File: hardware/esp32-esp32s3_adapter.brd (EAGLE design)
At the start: 21.9 x 26.9 mm, 5 parts, among them U1 ESP32-S3-WROOM-1-N16R2, U2 ESP32-WROOM-32E_(16MB)

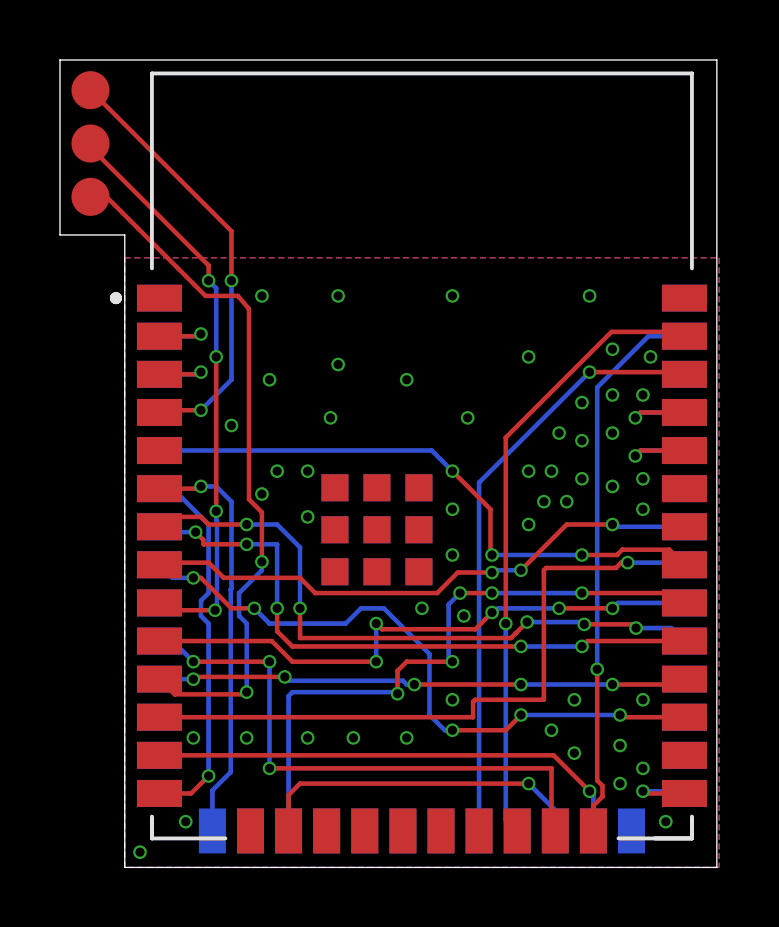
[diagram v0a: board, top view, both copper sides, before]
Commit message: Added RevB of ESP32toESP32S3 V1.4 and 2.0
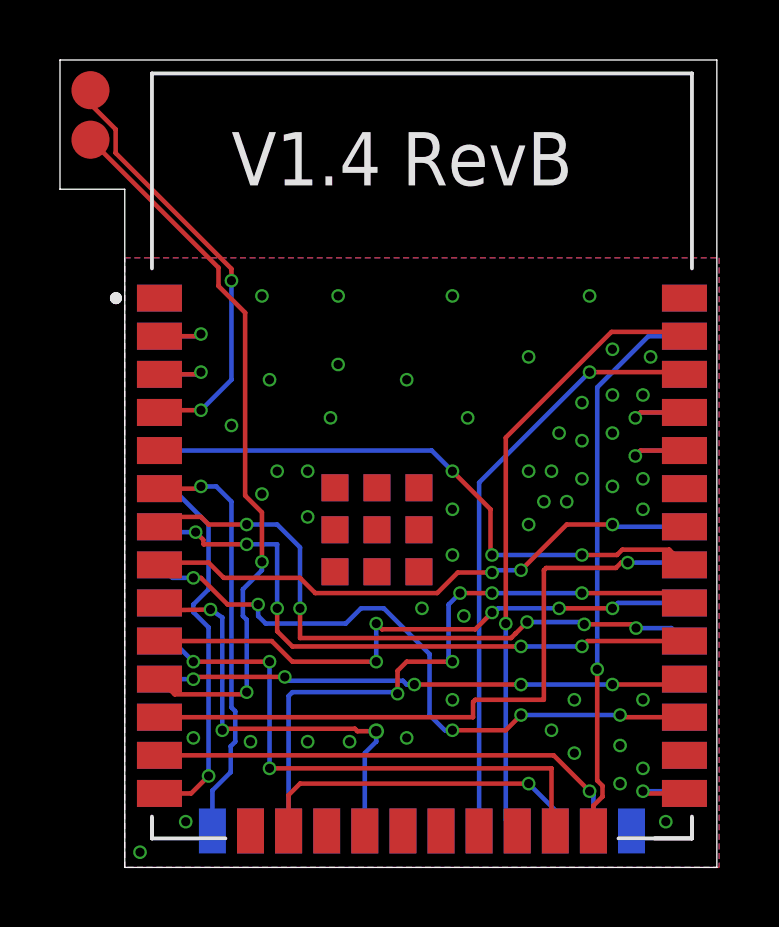
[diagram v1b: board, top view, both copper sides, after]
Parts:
- removed TP3: TPB1,27, testpad:B1,27
- moved TP1 1.91 mm to (2.41, 77.3)
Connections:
- net SQL: now also U1.19; no longer TP3.TP
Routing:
- net SQL: track 19.3 -> 14.7 mm, vias 4 -> 3
- net AF_OUT: track 23.4 -> 24.2 mm
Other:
- outline, holes or cut-outs redrawn
- board text added: "V1.4 RevB"

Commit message: RevC of ESP32-ESP32S3 Adapter SCH/PCB
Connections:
- removed net SCA: U1.21
- net SDA: now also U1.21
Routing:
- net SDA: track 0.00 -> 21.0 mm, vias 0 -> 3
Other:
- board text added: "V1.4 RevC"
- board text removed: "V1.4 RevB"
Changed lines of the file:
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@@
 <wire x1="1.397" y1="75.692" x2="3.556" y2="75.692" width="0" layer="20"/>
 <wire x1="3.556" y1="75.692" x2="3.556" y2="53.086" width="0" layer="20"/>
-<text x="7.112" y="75.819" size="1.778" layer="25">V1.4 RevB</text>
+<text x="7.112" y="75.819" size="1.778" layer="25">V1.4 RevC</text>
 </plain>
 <attributes>
@@
 <via x="11.049" y="57.277" extent="1-16" drill="0.3048"/>
 <via x="12.954" y="57.404" extent="1-16" drill="0.3048"/>
-<via x="17.78" y="57.658" extent="1-16" drill="0.3048"/>
 <via x="18.542" y="56.896" extent="1-16" drill="0.3048"/>
-<via x="20.066" y="57.15" extent="1-16" drill="0.3048"/>
 <via x="20.066" y="55.88" extent="1-16" drill="0.3048"/>
 <via x="20.828" y="56.388" extent="1-16" drill="0.3048"/>
 <via x="21.59" y="54.61" extent="1-16" drill="0.3048"/>
-<via x="20.828" y="58.674" extent="1-16" drill="0.3048"/>
 <via x="18.542" y="58.674" extent="1-16" drill="0.3048"/>
 <via x="20.828" y="68.834" extent="1-16" drill="0.3048"/>
-<via x="20.828" y="66.04" extent="1-16" drill="0.3048"/>
-<via x="20.828" y="65.024" extent="1-16" drill="0.3048"/>
-<via x="19.812" y="65.786" extent="1-16" drill="0.3048"/>
 <via x="19.812" y="67.564" extent="1-16" drill="0.3048"/>
 <via x="19.812" y="68.834" extent="1-16" drill="0.3048"/>
@@
 <via x="9.652" y="66.294" extent="1-16" drill="0.3048"/>
 <via x="14.478" y="63.5" extent="1-16" drill="0.3048"/>
-<via x="14.478" y="65.024" extent="1-16" drill="0.3048"/>
 <via x="8.128" y="72.136" extent="1-16" drill="0.3048"/>
 <via x="14.478" y="72.136" extent="1-16" drill="0.3048"/>
@@
 <via x="18.796" y="68.58" extent="1-16" drill="0.3048"/>
 <via x="18.796" y="67.31" extent="1-16" drill="0.3048"/>
-<via x="18.796" y="66.04" extent="1-16" drill="0.3048"/>
-<via x="18.288" y="65.278" extent="1-16" drill="0.3048"/>
-<via x="17.018" y="64.516" extent="1-16" drill="0.3048"/>
 <via x="17.018" y="66.294" extent="1-16" drill="0.3048"/>
 <via x="18.034" y="67.564" extent="1-16" drill="0.3048"/>
 <via x="17.78" y="66.294" extent="1-16" drill="0.3048"/>
-<via x="17.526" y="65.278" extent="1-16" drill="0.3048"/>
 <via x="21.082" y="70.104" extent="1-16" drill="0.3048"/>
 <via x="7.747" y="57.277" extent="1-16" drill="0.3048"/>
 <via x="5.842" y="57.404" extent="1-16" drill="0.3048"/>
-<via x="14.478" y="58.674" extent="1-16" drill="0.3048"/>
 <via x="13.462" y="61.722" extent="1-16" drill="0.3048"/>
-<via x="14.859" y="61.468" extent="1-16" drill="0.3048"/>
+<via x="14.478" y="65.024" extent="1-16" drill="0.3048"/>
+<via x="17.145" y="65.024" extent="1-16" drill="0.3048"/>
+<via x="17.018" y="64.135" extent="1-16" drill="0.3048"/>
+<via x="18.161" y="65.024" extent="1-16" drill="0.3048"/>
+<via x="19.939" y="65.151" extent="1-16" drill="0.3048"/>
 </signal>
 <signal name="BOOT_BTN">
@@
 <via x="14.478" y="59.944" extent="1-16" drill="0.3048"/>
 <wire x1="14.478" y1="59.944" x2="14.351" y2="60.071" width="0.1524" layer="16"/>
-<wire x1="14.351" y1="61.849" x2="14.351" y2="60.071" width="0.1524" layer="16"/>
-<wire x1="14.351" y1="61.849" x2="14.732" y2="62.23" width="0.1524" layer="16"/>
-<via x="14.732" y="62.23" extent="1-16" drill="0.3048"/>
+<wire x1="14.351" y1="61.976" x2="14.351" y2="60.071" width="0.1524" layer="16"/>
+<wire x1="14.351" y1="61.976" x2="14.605" y2="62.23" width="0.1524" layer="16"/>
+<via x="14.605" y="62.23" extent="1-16" drill="0.3048"/>
 <via x="15.7988" y="62.23" extent="1-16" drill="0.3048"/>
-<wire x1="14.732" y1="62.23" x2="15.7988" y2="62.23" width="0.1524" layer="1"/>
+<wire x1="14.605" y1="62.23" x2="15.7988" y2="62.23" width="0.1524" layer="1"/>
 <wire x1="15.7988" y1="62.23" x2="18.796" y2="62.23" width="0.1524" layer="16"/>
 <via x="18.796" y="62.23" extent="1-16" drill="0.3048"/>
@@
 <wire x1="12.5973375" y1="58.87666875" x2="12.5973375" y2="58.928" width="0.1524" layer="16"/>
 </signal>
-<signal name="SCA">
-<contactref element="U1" pad="21"/>
-</signal>
 <signal name="SCL">
 <contactref element="U1" pad="22"/>
@@
 <contactref element="U1" pad="8"/>
 <contactref element="U2" pad="27"/>
-<wire x1="22.212" y1="58.092" x2="20.14" y2="58.092" width="0.1524" layer="1"/>
-<wire x1="20.14" y1="58.092" x2="20.066" y2="58.166" width="0.1524" layer="1"/>
-<via x="20.066" y="58.166" extent="1-16" drill="0.3048"/>
-<wire x1="20.066" y1="58.166" x2="16.764" y2="58.166" width="0.1524" layer="16"/>
+<wire x1="22.212" y1="58.092" x2="20.648" y2="58.092" width="0.1524" layer="1"/>
+<wire x1="20.648" y1="58.092" x2="20.574" y2="58.166" width="0.1524" layer="1"/>
+<via x="20.574" y="58.166" extent="1-16" drill="0.3048"/>
+<wire x1="20.574" y1="58.166" x2="16.764" y2="58.166" width="0.1524" layer="16"/>
 <via x="16.764" y="58.166" extent="1-16" drill="0.3048"/>
 <wire x1="16.764" y1="58.166" x2="16.256" y2="57.658" width="0.1524" layer="1"/>
@@
 <contactref element="U1" pad="32"/>
 <contactref element="U2" pad="10"/>
-<wire x1="22.212" y1="61.902" x2="19.992" y2="61.902" width="0.1524" layer="16"/>
-<wire x1="19.992" y1="61.902" x2="19.812" y2="61.722" width="0.1524" layer="16"/>
-<via x="19.812" y="61.722" extent="1-16" drill="0.3048"/>
+<wire x1="22.212" y1="61.902" x2="20.754" y2="61.902" width="0.1524" layer="16"/>
+<wire x1="20.754" y1="61.902" x2="20.574" y2="61.722" width="0.1524" layer="16"/>
+<via x="20.574" y="61.722" extent="1-16" drill="0.3048"/>
 <wire x1="4.712" y1="60.632" x2="8.456" y2="60.632" width="0.1524" layer="1"/>
 <wire x1="8.456" y1="60.632" x2="9.144" y2="59.944" width="0.1524" layer="1"/>
@@
 <wire x1="11.938" y1="59.944" x2="11.938" y2="61.214" width="0.1524" layer="16"/>
 <via x="11.938" y="61.214" extent="1-16" drill="0.3048"/>
-<wire x1="19.812" y1="61.722" x2="18.034" y2="61.722" width="0.1524" layer="1"/>
+<wire x1="20.574" y1="61.722" x2="18.034" y2="61.722" width="0.1524" layer="1"/>
 <via x="18.034" y="61.722" extent="1-16" drill="0.3048"/>
 <wire x1="18.034" y1="61.722" x2="16.002" y2="61.722" width="0.1524" layer="16"/>
@@
 <contactref element="U2" pad="12"/>
 <wire x1="15.166" y1="58.092" x2="4.712" y2="58.092" width="0.1524" layer="1"/>
-<via x="20.32" y="63.246" extent="1-16" drill="0.3048"/>
-<wire x1="20.32" y1="63.246" x2="22.138" y2="63.246" width="0.1524" layer="16"/>
+<via x="20.574" y="63.246" extent="1-16" drill="0.3048"/>
+<wire x1="20.574" y1="63.246" x2="22.138" y2="63.246" width="0.1524" layer="16"/>
 <wire x1="22.138" y1="63.246" x2="22.212" y2="63.172" width="0.1524" layer="16"/>
-<wire x1="20.32" y1="63.246" x2="20.104475" y2="63.246" width="0.1524" layer="1"/>
+<wire x1="20.574" y1="63.246" x2="20.104475" y2="63.246" width="0.1524" layer="1"/>
 <wire x1="17.6022" y1="63.0682" x2="17.526" y2="62.992" width="0.1524" layer="1"/>
 <wire x1="20.104475" y1="63.246" x2="19.926675" y2="63.0682" width="0.1524" layer="1"/>
@@
 <contactref element="U1" pad="34"/>
 <contactref element="U2" pad="8"/>
-<wire x1="22.212" y1="64.442" x2="19.886" y2="64.442" width="0.1524" layer="16"/>
-<wire x1="19.886" y1="64.442" x2="19.812" y2="64.516" width="0.1524" layer="16"/>
-<via x="19.812" y="64.516" extent="1-16" drill="0.3048"/>
-<wire x1="19.812" y1="64.516" x2="18.288" y2="64.516" width="0.1524" layer="1"/>
+<wire x1="22.212" y1="64.442" x2="20.648" y2="64.442" width="0.1524" layer="16"/>
+<wire x1="20.648" y1="64.442" x2="20.574" y2="64.516" width="0.1524" layer="16"/>
+<via x="20.574" y="64.516" extent="1-16" drill="0.3048"/>
+<wire x1="20.574" y1="64.516" x2="18.288" y2="64.516" width="0.1524" layer="1"/>
 <wire x1="18.288" y1="64.516" x2="16.764" y2="62.992" width="0.1524" layer="1"/>
 <via x="16.764" y="62.992" extent="1-16" drill="0.3048"/>
@@
 <contactref element="U1" pad="11"/>
 <wire x1="22.212" y1="59.362" x2="22.032" y2="59.182" width="0.1524" layer="1"/>
-<wire x1="22.032" y1="59.182" x2="19.812" y2="59.182" width="0.1524" layer="1"/>
-<via x="19.812" y="59.182" extent="1-16" drill="0.3048"/>
-<wire x1="19.812" y1="59.182" x2="16.764" y2="59.182" width="0.1524" layer="16"/>
+<wire x1="22.032" y1="59.182" x2="20.574" y2="59.182" width="0.1524" layer="1"/>
+<via x="20.574" y="59.182" extent="1-16" drill="0.3048"/>
+<wire x1="20.574" y1="59.182" x2="16.764" y2="59.182" width="0.1524" layer="16"/>
 <via x="16.764" y="59.182" extent="1-16" drill="0.3048"/>
 <via x="13.208" y="59.182" extent="1-16" drill="0.3048"/>
@@
 <signal name="SDA">
 <contactref element="U2" pad="33"/>
+<contactref element="U1" pad="21"/>
+<wire x1="14.097" y1="54.302" x2="14.097" y2="54.737" width="0.1524" layer="16"/>
+<wire x1="14.097" y1="54.737" x2="15.0876" y2="55.7276" width="0.1524" layer="16"/>
+<wire x1="15.8242" y1="65.7595375" x2="18.8965375" y2="65.7595375" width="0.1524" layer="16"/>
+<wire x1="18.8965375" y1="65.7595375" x2="18.923" y2="65.786" width="0.1524" layer="16"/>
+<wire x1="18.923" y1="65.786" x2="18.8722" y2="65.786" width="0.1524" layer="16"/>
+<via x="18.8722" y="65.786" extent="1-16" drill="0.3048"/>
+<wire x1="20.066" y1="65.786" x2="18.8722" y2="65.786" width="0.1524" layer="1"/>
+<wire x1="22.212" y1="65.712" x2="20.14" y2="65.712" width="0.1524" layer="1"/>
+<wire x1="20.14" y1="65.712" x2="20.066" y2="65.786" width="0.1524" layer="1"/>
+<wire x1="15.0876" y1="55.7276" x2="15.0876" y2="66.0287375" width="0.1524" layer="16"/>
+<wire x1="15.748" y1="66.6891375" x2="15.748" y2="66.802" width="0.1524" layer="16"/>
+<wire x1="15.0876" y1="66.0287375" x2="15.748" y2="66.6891375" width="0.1524" layer="16"/>
+<wire x1="15.748" y1="66.802" x2="15.69666875" y2="66.85333125" width="0.1524" layer="16"/>
+<via x="15.69666875" y="66.85333125" extent="1-16" drill="0.3048"/>
+<wire x1="15.69666875" y1="66.85333125" x2="15.69666875" y2="65.83733125" width="0.1524" layer="1"/>
+<wire x1="15.7744625" y1="65.7595375" x2="15.8242" y2="65.7595375" width="0.1524" layer="1"/>
+<via x="15.8242" y="65.7595375" extent="1-16" drill="0.3048"/>
+<wire x1="15.69666875" y1="65.83733125" x2="15.7744625" y2="65.7595375" width="0.1524" layer="1"/>
 </signal>
 <signal name="AF_OUT">
